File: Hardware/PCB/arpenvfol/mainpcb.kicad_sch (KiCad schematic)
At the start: 58 parts, among them J3 AudioJack2_SwitchT, J4 AudioJack2_SwitchT, J5 AudioJack2, J6 AudioJack2, Q1 2N3904, Q2 2N3904, U1 TL074

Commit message: README edit; design updates; panel art
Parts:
- U1: footprint (none) -> ao_tht:DIP-14_W7.62mm_Socket_LongPads; symbol Amplifier_Operational:TL074 -> ao_symbols:TL074; SKU (none) -> A-1138; Vendor (none) -> Tayda
- gave numbers to parts that had none: 2

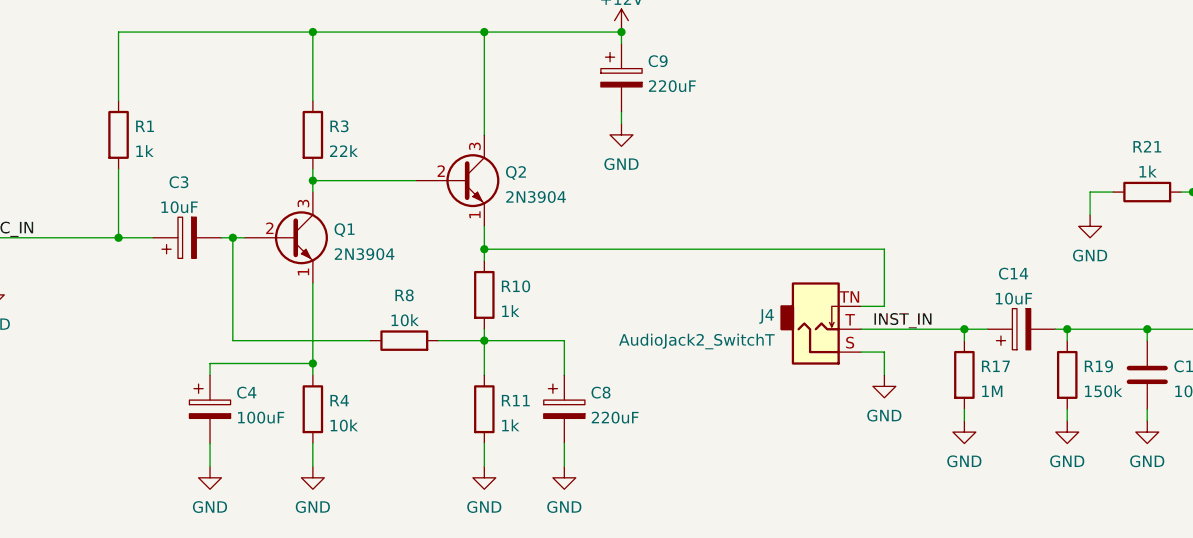
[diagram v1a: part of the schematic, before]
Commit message: NP electrolytics; revise panel
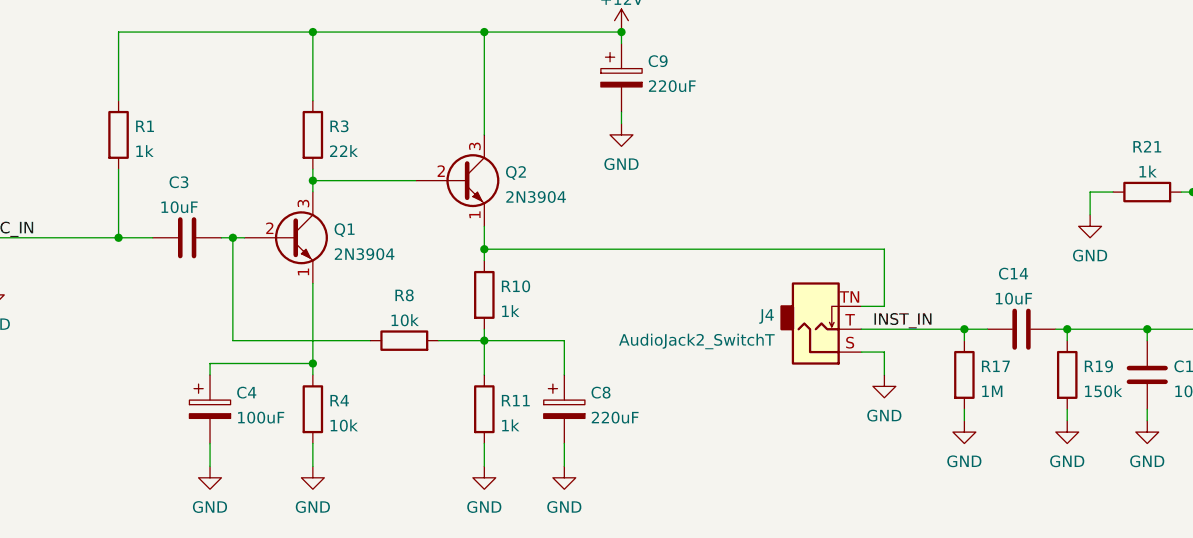
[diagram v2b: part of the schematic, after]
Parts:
- C14, C3: footprint ao_tht:CP_Radial_D6.3mm_P2.50mm -> ao_tht:C_Radial_D8.0mm_H11.5mm_P3.50mm; symbol ao_symbols:CP -> ao_symbols:C; SKU (none) -> A-4349
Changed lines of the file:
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@@
     (pin "2")
   )
-  (symbol (lib_id "ao_symbols:CP") (at 74.93 135.89 90) (unit 1)
+  (symbol (lib_id "ao_symbols:C") (at 74.93 135.89 90) (unit 1)
     (in_bom yes) (on_board yes) (fields_autoplaced)
     (property "Reference" "C3" (id 0) (at 74.041 129.7645 90))
     (property "Value" "10uF" (id 1) (at 74.041 132.5396 90))
-    (property "Footprint" "ao_tht:CP_Radial_D6.3mm_P2.50mm" (id 2) (at 78.74 134.9248 0)
+    (property "Footprint" "ao_tht:C_Radial_D8.0mm_H11.5mm_P3.50mm" (id 2) (at 78.74 134.9248 0)
       (effects (font (size 1.27 1.27)) hide)
     )
@@
     )
     (property "Vendor" "Tayda" (id 4) (at 74.93 135.89 0)
+      (effects (font (size 1.27 1.27)) hide)
+    )
+    (property "SKU" "A-4349" (id 5) (at 74.93 135.89 90)
       (effects (font (size 1.27 1.27)) hide)
     )
@@
     (pin "2")
   )
-  (symbol (lib_id "ao_symbols:CP") (at 167.64 146.05 90) (unit 1)
+  (symbol (lib_id "ao_symbols:C") (at 167.64 146.05 90) (unit 1)
     (in_bom yes) (on_board yes) (fields_autoplaced)
     (property "Reference" "C14" (id 0) (at 166.751 139.9245 90))
     (property "Value" "10uF" (id 1) (at 166.751 142.6996 90))
-    (property "Footprint" "ao_tht:CP_Radial_D6.3mm_P2.50mm" (id 2) (at 171.45 145.0848 0)
+    (property "Footprint" "ao_tht:C_Radial_D8.0mm_H11.5mm_P3.50mm" (id 2) (at 171.45 145.0848 0)
       (effects (font (size 1.27 1.27)) hide)
     )
@@
       (effects (font (size 1.27 1.27)) hide)
     )
+    (property "SKU" "A-4349" (id 5) (at 167.64 146.05 90)
+      (effects (font (size 1.27 1.27)) hide)
+    )

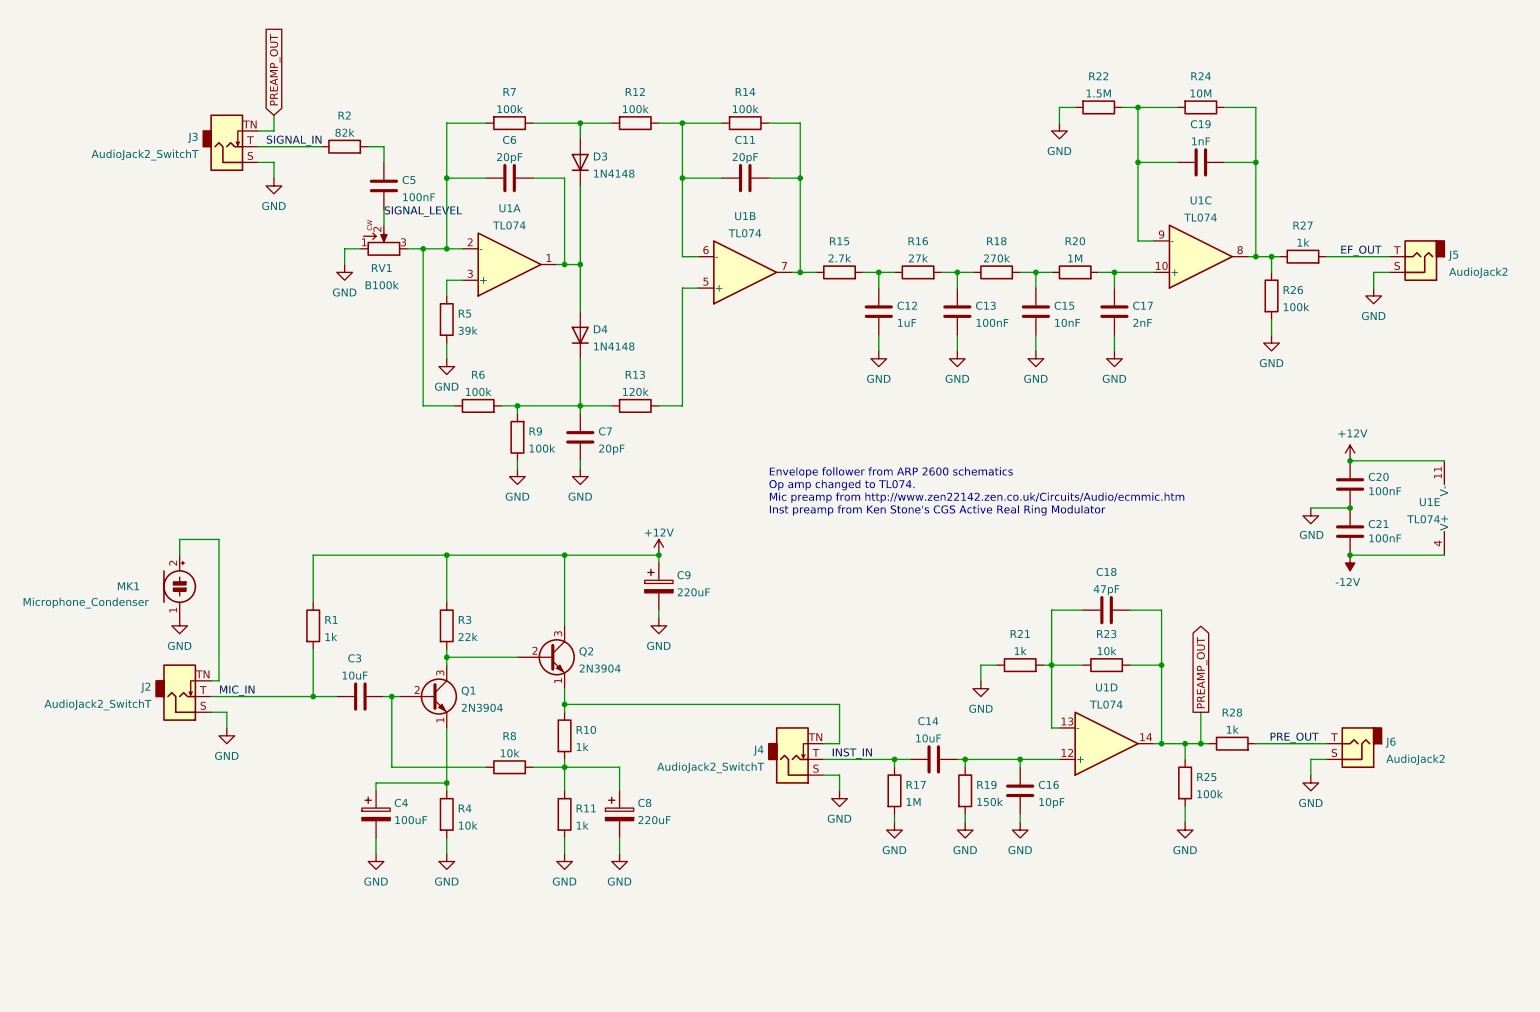
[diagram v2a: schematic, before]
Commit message: Better .gitignore; misc revisions
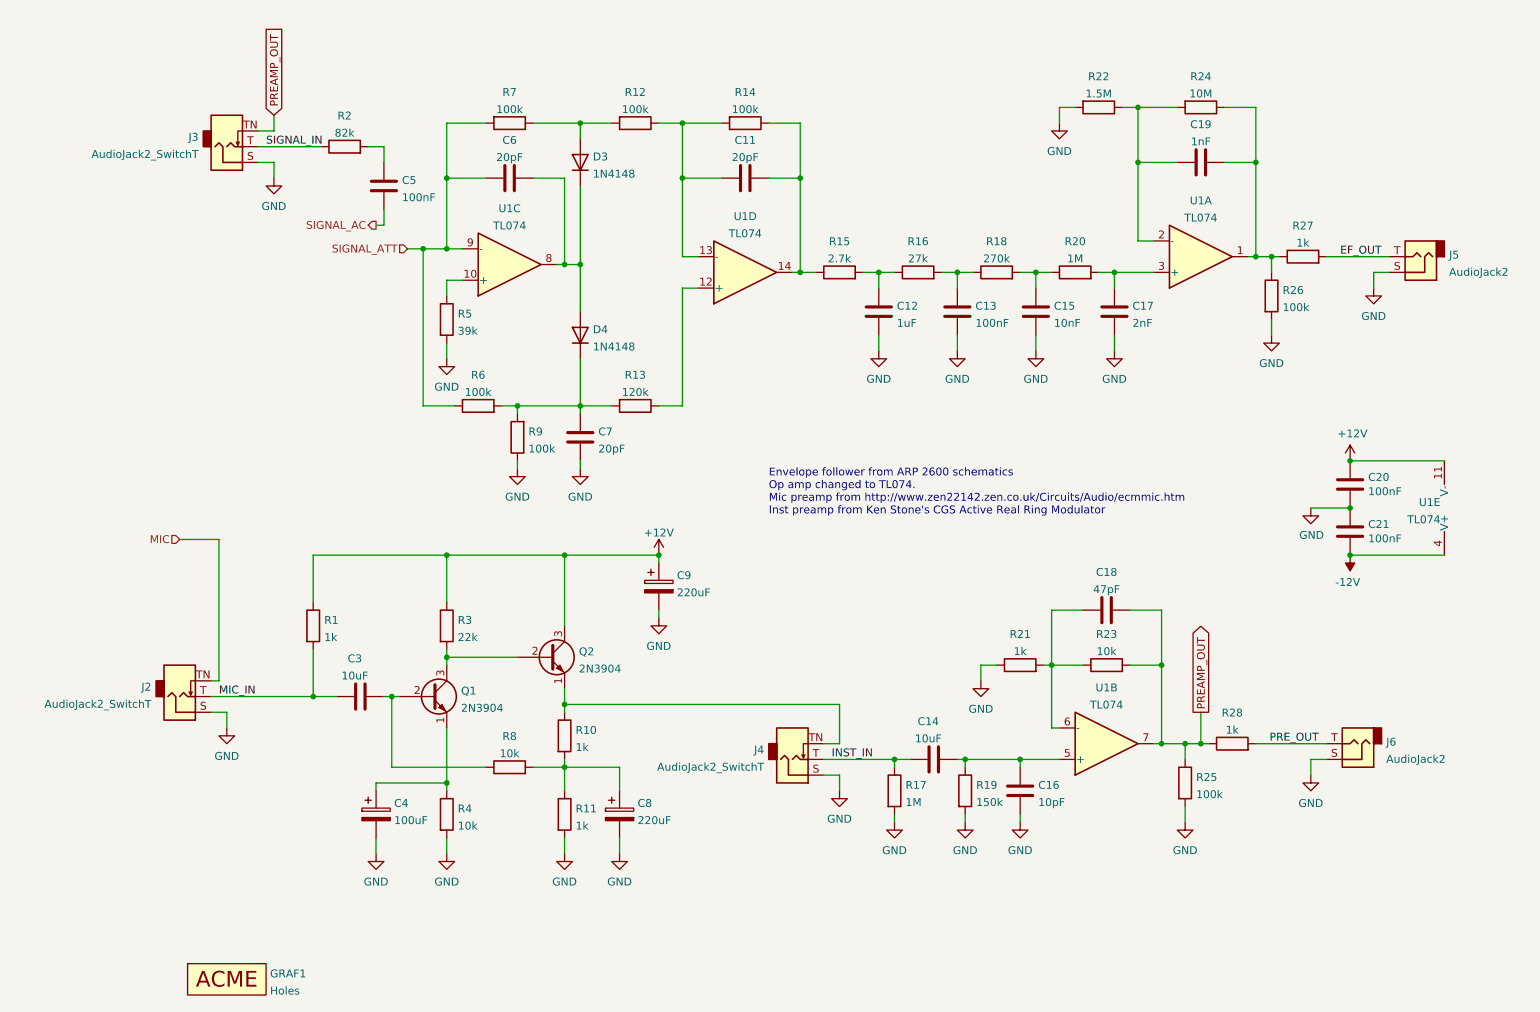
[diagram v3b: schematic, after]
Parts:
- removed MK1: Microphone_Condenser, symbol Device:Microphone_Condenser
- removed RV1: B100k, symbol ao_symbols:R_POT
- added GRAF1: Holes, arpenvfol:arpenvfol_panel_holes, symbol ao_symbols:Graphic
- C12, C13, C15, C17, C19, C5: footprint ao_tht:C_Disc_D3.0mm_W1.6mm_P2.50mm -> ao_tht:C_Rect_L7.2mm_W2.5mm_P5.00mm_FKS2_FKP2_MKS2_MKP2
- J2, J3, J4, J5, J6: footprint (none) -> ao_tht:Jack_6.35mm_PJ_629HAN_slots
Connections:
- net PREAMP_OUT: now also U1.7; no longer U1.14
- net MIC: now reaches J2.TN
- net at C11.2, R14.1, R15.1: now also U1.14; no longer U1.7
- net at C11.1, R12.1, R14.2: now also U1.13 (-); no longer U1.6 (-)
- net at C18.1, R21.2, R23.1: now also U1.6 (-); no longer U1.13 (-)
- net at C17.1, R20.2: now also U1.3 (+); no longer U1.10 (+)
- net at R5.1: now also U1.10 (+); no longer U1.3 (+)
- net at C14.2, C16.1, R19.1: now also U1.5 (+); no longer U1.12 (+)
- net at C19.1, R22.1, R24.2: now also U1.2 (-); no longer U1.9 (-)
- net at C19.2, R24.1, R26.1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: now also U1.1; no longer U1.8
- net at R13.1: now also U1.12 (+); no longer U1.5 (+)
- net at C6.2, D3.1 (K), D4.2 (A): now also U1.8; no longer U1.1
- net SIGNAL_ATT: now reaches C6.1, R6.1, R7.2
- net SIGNAL_ATT: now also U1.9 (-); no longer U1.2 (-)
- net SIGNAL_LEVEL renamed SIGNAL_AC
